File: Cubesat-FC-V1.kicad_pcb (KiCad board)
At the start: 2 copper layers, 109 parts, among them SW1 SW_Button, SW2 SW_SPDT, SW3 SW_SPDT, U1 MMC5983MA, U10 W25Q128JVS, U11 W25Q128JVS, U3 W25Q128JVS, U5 STM32H757BITx, U8 W25Q128JVS, U9 W25Q128JVS, Y1 ASCO, Y3 ASE-xxxMHz

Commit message: Beginnings of routing
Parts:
- removed the D1 at (136.2, 69.5)
- removed the D1 at (141.4, 100.2)
- removed the D2 at (136.2, 72.1)
- removed the D2 at (141.4, 102.8)
- removed the D3 at (141.4, 105.4)
- removed the D3 at (136.2, 74.7)
- removed the D4 at (141.4, 108.0)
- removed the D4 at (136.2, 77.2)
- removed the D5 at (136.2, 79.8)
- removed the D5 at (141.4, 110.6)
- removed the D6 at (136.2, 82.4)
- removed the D6 at (141.4, 113.2)
- removed JP1, JP4: Jumper, Jumper:SolderJumper-3_P1.3mm_Open_RoundedPad1.0x1.5mm
- removed the JP2 at (146.2, 100.7)
- removed the JP2 at (141.1, 79.8)
- removed the R1 at (137.9, 99.9)
- removed the R1 at (139.7, 71.2)
- removed the R3 at (137.9, 101.9)
- removed the R3 at (142.6, 69.2)
- removed the R4 at (142.6, 71.2)
- removed the R4 at (137.9, 103.9)
- removed the R5 at (137.9, 105.9)
- removed the R5 at (142.6, 73.2)
- removed the R6 at (137.9, 107.9)
- removed the R6 at (145.5, 69.2)
- removed the R7 at (137.9, 109.9)
- removed the R7 at (145.5, 71.2)
- removed the R8 at (137.9, 111.9)
- removed the R8 at (145.5, 73.2)
- removed the SW1 at (141.6, 84.2)
- removed the SW1 at (152.4, 112.4)
- added BZ1: Buzzer, Buzzer_Beeper:Buzzer_Murata_PKMCS0909E, F.Cu at (20.0, 22.0)
- added C59: 10n, Capacitor_SMD:C_0402_1005Metric, F.Cu at (156.1, 112.4)
- added C60: 2.2u, Capacitor_SMD:C_0402_1005Metric, F.Cu at (154.2, 118.4)
- added C61: 0.1u, Capacitor_SMD:C_0402_1005Metric, F.Cu at (156.1, 118.4)
- added C62: 10n, Capacitor_SMD:C_0402_1005Metric, F.Cu at (156.1, 119.4)
- added C63: 10u, Capacitor_SMD:C_0402_1005Metric, F.Cu at (164.3, 104.6)
- added C64: 1u, Capacitor_SMD:C_0402_1005Metric, F.Cu at (164.4, 120.4)
- added C65: 10n, Capacitor_SMD:C_0402_1005Metric, F.Cu at (162.5, 110.0)
- added C66: 0.1u, Capacitor_SMD:C_0402_1005Metric, B.Cu at (136.2, 78.9)
- added C67: 0.1u, Capacitor_SMD:C_0402_1005Metric, B.Cu at (136.2, 84.9)
- added C68: 0.1u, Capacitor_SMD:C_0402_1005Metric, B.Cu at (137.5, 89.4)
- added C69: 0.1u, Capacitor_SMD:C_0402_1005Metric, B.Cu at (136.2, 96.9)
- added C70: 10u, Capacitor_SMD:C_0402_1005Metric, B.Cu at (138.9, 67.9)
- added C71: 10u, Capacitor_SMD:C_0402_1005Metric, F.Cu at (141.9, 63.8)
- added C72: 10u, Capacitor_SMD:C_0402_1005Metric, B.Cu at (132.9, 67.9)
- added C73: 10u, Capacitor_SMD:C_0402_1005Metric, F.Cu at (135.9, 63.8)
- added C74: 10u, Capacitor_SMD:C_0402_1005Metric, F.Cu at (86.2, 93.8)
- added C75: 0.1u, Capacitor_SMD:C_0402_1005Metric, F.Cu at (86.2, 95.8)
- added C76: 0.1u, Capacitor_SMD:C_0402_1005Metric, F.Cu at (86.2, 97.8)
- added C77: 10u, Capacitor_SMD:C_0402_1005Metric, F.Cu at (86.2, 99.7)
- added D1: LED_G, LED_SMD:LED_0603_1608Metric, F.Cu at (17.8, 28.5)
- added D2: LED_G, LED_SMD:LED_0603_1608Metric, F.Cu at (17.8, 31.1)
- added D3: LED_G, LED_SMD:LED_0603_1608Metric, F.Cu at (17.8, 33.6)
- added D4: LED_G, LED_SMD:LED_0603_1608Metric, F.Cu at (17.8, 36.2)
- added D5: LED_G, LED_SMD:LED_0603_1608Metric, F.Cu at (17.8, 38.8)
- added D6: LED_G, LED_SMD:LED_0603_1608Metric, F.Cu at (17.8, 41.4)
- added D7: LED_G, LED_SMD:LED_0603_1608Metric, F.Cu at (89.7, 100.4)
- added D8: LED_R, LED_SMD:LED_0603_1608Metric, F.Cu at (89.7, 103.0)
- added H1: M3, MountingHole:MountingHole_3.2mm_M3_ISO7380_Pad_TopBottom, F.Cu at (113.5, 58.5)
- added H2: M3, MountingHole:MountingHole_3.2mm_M3_ISO7380_Pad_TopBottom, F.Cu at (113.5, 123.5)
- added H3: M3, MountingHole:MountingHole_3.2mm_M3_ISO7380_Pad_TopBottom, F.Cu at (169.5, 58.5)
- added H4: M3, MountingHole:MountingHole_3.2mm_M3_ISO7380_Pad_TopBottom, F.Cu at (169.5, 123.5)
- added J1: Conn_01x03_Pin, Connector_Molex:Molex_Micro-Latch_53253-0370_1x03_P2.00mm_Vertical, F.Cu at (19.1, 82.6)
- added J10: Conn_01x04_Pin, Connector_Molex:Molex_Micro-Latch_53253-0470_1x04_P2.00mm_Vertical, F.Cu at (19.1, 44.8)
- added J11: USB_C_Receptacle_USB2.0_14P, Connector_USB:USB_C_Receptacle_GCT_USB4105-xx-A_16P_TopMnt_Horizontal, F.Cu at (42.0, 74.7)
- added J12: Conn_01x03_Pin, Connector_Molex:Molex_Micro-Latch_53253-0370_1x03_P2.00mm_Vertical, F.Cu at (71.0, 62.4)
- added J13: Conn_01x03_Pin, Connector_Molex:Molex_Micro-Latch_53253-0370_1x03_P2.00mm_Vertical, F.Cu at (71.0, 68.1)
- added J14: Conn_01x03_Pin, Connector_Molex:Molex_Micro-Latch_53253-0370_1x03_P2.00mm_Vertical, F.Cu at (71.0, 73.8)
- added J15: Conn_01x03_Pin, Connector_Molex:Molex_Micro-Latch_53253-0370_1x03_P2.00mm_Vertical, F.Cu at (71.0, 79.5)
- added J3: Conn_01x03_Pin, Connector_Molex:Molex_Micro-Latch_53253-0370_1x03_P2.00mm_Vertical, F.Cu at (19.1, 88.3)
- added J4: Conn_01x04_Pin, Connector_Molex:Molex_Micro-Latch_53253-0470_1x04_P2.00mm_Vertical, F.Cu at (19.1, 49.8)
- added J5: Conn_01x04_Pin, Connector_Molex:Molex_Micro-Latch_53253-0470_1x04_P2.00mm_Vertical, F.Cu at (19.1, 55.5)
- added J6: Conn_01x04_Pin, Connector_Molex:Molex_Micro-Latch_53253-0470_1x04_P2.00mm_Vertical, F.Cu at (19.1, 61.2)
- added J7: USB_C_Receptacle_USB2.0_14P, Connector_USB:USB_C_Receptacle_GCT_USB4105-xx-A_16P_TopMnt_Horizontal, F.Cu at (21.9, 75.4)
- added J8: Conn_01x04_Pin, Connector_Molex:Molex_Micro-Latch_53253-0470_1x04_P2.00mm_Vertical, F.Cu at (19.1, 66.9)
- added J9: Micro_SD_Card, Connector_Card:microSD_HC_Hirose_DM3D-SF, F.Cu at (166.4, 95.5)
- added JP2: Jumper_3_Open, Jumper:SolderJumper-3_P1.3mm_Open_RoundedPad1.0x1.5mm, F.Cu at (45.1, 15.9)
- added JP6: Jumper, Jumper:SolderJumper-3_P1.3mm_Open_RoundedPad1.0x1.5mm, F.Cu at (49.1, 38.4)
- added JP7: Jumper, Jumper:SolderJumper-3_P1.3mm_Open_RoundedPad1.0x1.5mm, F.Cu at (54.8, 30.7)
- added JP8: Jumper, Jumper:SolderJumper-3_P1.3mm_Open_RoundedPad1.0x1.5mm, F.Cu at (54.8, 34.5)
- added JP9: Jumper, Jumper:SolderJumper-3_P1.3mm_Open_RoundedPad1.0x1.5mm, F.Cu at (54.8, 38.4)
- added R1: R_Small, Resistor_SMD:R_0402_1005Metric, F.Cu at (21.6, 28.4)
- added R10: 1k, Resistor_SMD:R_0402_1005Metric, F.Cu at (18.8, 125.5)
- added R11: R_Small, Resistor_SMD:R_0402_1005Metric, F.Cu at (18.8, 127.5)
- added R12: 100, Resistor_SMD:R_0402_1005Metric, F.Cu at (61.5, 15.9)
- added R13: 30.9k, Resistor_SMD:R_0402_1005Metric, F.Cu at (37.3, 122.0)
- added R14: 10k, Resistor_SMD:R_0402_1005Metric, F.Cu at (37.3, 124.0)
- added R15: 68k, Resistor_SMD:R_0402_1005Metric, F.Cu at (37.3, 126.0)
- added R16: R_Small, Resistor_SMD:R_0402_1005Metric, F.Cu at (44.0, 37.2)
- added R17: R_Small, Resistor_SMD:R_0402_1005Metric, F.Cu at (44.0, 39.2)
- added R18: 120, Resistor_SMD:R_0402_1005Metric, F.Cu at (138.9, 62.7)
- added R19: 120, Resistor_SMD:R_0402_1005Metric, F.Cu at (132.9, 62.7)
- added R20: 20k, Resistor_SMD:R_0402_1005Metric, F.Cu at (83.3, 93.8)
- added R21: 47k, Resistor_SMD:R_0402_1005Metric, F.Cu at (83.3, 95.8)
- added R22: 20k, Resistor_SMD:R_0402_1005Metric, F.Cu at (83.3, 97.8)
- added R23: 20k, Resistor_SMD:R_0402_1005Metric, F.Cu at (83.3, 99.8)
- added R24: 5.1k, Resistor_SMD:R_0402_1005Metric, F.Cu at (37.6, 80.4)
- added R25: 5.1k, Resistor_SMD:R_0402_1005Metric, F.Cu at (37.6, 82.4)
- added R3: R_Small, Resistor_SMD:R_0402_1005Metric, F.Cu at (21.6, 32.4)
- added R4: R_Small, Resistor_SMD:R_0402_1005Metric, F.Cu at (21.6, 34.4)
- added R5: R_Small, Resistor_SMD:R_0402_1005Metric, F.Cu at (21.6, 36.4)
- added R6: R_Small, Resistor_SMD:R_0402_1005Metric, F.Cu at (21.6, 38.4)
- added R7: 5.1k, Resistor_SMD:R_0402_1005Metric, F.Cu at (14.7, 71.2)
- added R8: 5.1k, Resistor_SMD:R_0402_1005Metric, F.Cu at (14.7, 73.2)
- added SW1: SW_SPDT, Button_Switch_THT:SW_CK_JS202011CQN_DPDT_Straight, F.Cu at (61.6, 18.1)
- added SW4: SW_Button, Button_Switch_SMD:SW_SPST_PTS810, F.Cu at (37.9, 38.1)
- added SW5: SW_SPDT, Button_Switch_THT:SW_CK_JS202011CQN_DPDT_Straight, F.Cu at (36.0, 25.2)
- added SW6: SW_SPDT, Button_Switch_THT:SW_CK_JS202011CQN_DPDT_Straight, F.Cu at (36.0, 30.8)
- added TP1: TestPoint, TestPoint:TestPoint_Pad_D1.5mm, F.Cu at (16.4, 101.5)
- added TP10: TestPoint, TestPoint:TestPoint_Pad_D1.5mm, F.Cu at (27.0, 97.6)
- added TP11: TestPoint, TestPoint:TestPoint_Pad_D1.5mm, F.Cu at (27.0, 101.2)
- added TP12: TestPoint, TestPoint:TestPoint_Pad_D1.5mm, F.Cu at (27.0, 104.7)
- added TP13: TestPoint, TestPoint:TestPoint_Pad_D1.5mm, F.Cu at (30.6, 87.0)
- added TP14: TestPoint, TestPoint:TestPoint_Pad_D1.5mm, F.Cu at (30.6, 90.5)
- added TP15: TestPoint, TestPoint:TestPoint_Pad_D1.5mm, F.Cu at (30.6, 94.0)
- added TP16: TestPoint, TestPoint:TestPoint_Pad_D1.5mm, F.Cu at (30.6, 97.6)
- added TP17: TestPoint, TestPoint:TestPoint_Pad_D1.5mm, F.Cu at (30.6, 101.2)
- added TP18: TestPoint, TestPoint:TestPoint_Pad_D1.5mm, F.Cu at (30.6, 104.7)
- added TP19: TestPoint, TestPoint:TestPoint_Pad_D1.5mm, F.Cu at (34.1, 87.0)
- added TP2: TestPoint, TestPoint:TestPoint_Pad_D1.5mm, F.Cu at (16.4, 105.0)
- added TP20: TestPoint, TestPoint:TestPoint_Pad_D1.5mm, F.Cu at (34.1, 90.5)
- added TP21: TestPoint, TestPoint:TestPoint_Pad_D1.5mm, F.Cu at (34.1, 94.0)
- added TP22: TestPoint, TestPoint:TestPoint_Pad_D1.5mm, F.Cu at (34.1, 97.6)
- added TP23: TestPoint, TestPoint:TestPoint_Pad_D1.5mm, F.Cu at (34.1, 101.2)
- added TP24: TestPoint, TestPoint:TestPoint_Pad_D1.5mm, F.Cu at (34.1, 104.7)
- added TP3: TestPoint, TestPoint:TestPoint_Pad_D1.5mm, F.Cu at (19.9, 101.5)
- added TP4: TestPoint, TestPoint:TestPoint_Pad_D1.5mm, F.Cu at (19.9, 105.0)
- added TP5: TestPoint, TestPoint:TestPoint_Pad_D1.5mm, F.Cu at (23.5, 101.5)
- added TP6: TestPoint, TestPoint:TestPoint_Pad_D1.5mm, F.Cu at (23.5, 105.0)
- added TP7: TestPoint, TestPoint:TestPoint_Pad_D1.5mm, F.Cu at (27.0, 87.0)
- added TP8: TestPoint, TestPoint:TestPoint_Pad_D1.5mm, F.Cu at (27.0, 90.5)
- added TP9: TestPoint, TestPoint:TestPoint_Pad_D1.5mm, F.Cu at (27.0, 94.0)
- added U12: W25Q128JVS, Package_SO:SOIC-8_5.3x5.3mm_P1.27mm, B.Cu at (141.4, 80.4)
- added U13: W25Q128JVS, Package_SO:SOIC-8_5.3x5.3mm_P1.27mm, B.Cu at (141.4, 92.4)
- added U14: W25Q128JVS, Package_SO:SOIC-8_5.3x5.3mm_P1.27mm, B.Cu at (141.4, 98.4)
- added U15: MCP2558FD, Package_SO:SOIC-8_3.9x4.9mm_P1.27mm, F.Cu at (138.9, 67.0)
- added U16: MCP2558FD, Package_SO:SOIC-8_3.9x4.9mm_P1.27mm, F.Cu at (132.9, 67.0)
- added U18: CP2102N-Axx-xQFN24, Package_DFN_QFN:QFN-24-1EP_4x4mm_P0.5mm_EP2.6x2.6mm, F.Cu at (90.8, 96.0)
- added U4: STM32H757BITx, Package_QFP:LQFP-208_28x28mm_P0.5mm, F.Cu at (141.0, 89.5)
- added Y2: ASCO, Oscillator:Oscillator_SMD_Abracon_ASCO-4Pin_1.6x1.2mm, F.Cu at (124.3, 93.2)
- C10, C11: value 0.1u -> 100u; footprint Capacitor_SMD:C_0402_1005Metric -> Capacitor_SMD:C_1206_3216Metric
- C2, C8, C9: value 0.1u -> 47u; footprint Capacitor_SMD:C_0402_1005Metric -> Capacitor_SMD:C_1206_3216Metric
- C24, C30, C50: value 1u -> 0.1u
- C25, C26, C27, C28: value 2.2u -> 0.1u
- C3, C7: value 0.1u -> 10u
- C32: value 4.7u -> 0.1u
- C33, C34: value ?? -> 0.1u
- C38: value 10n -> 0.1u
- C39: value 0.1u -> 4.7u
- C40: value 10n -> 1u
- C41, C44, C57: value 0.1u -> 2.2u
- C43: value 10n -> 2.2u
- C45: value 2.2u -> 1u
- C46: value 10u -> 0.1u
- C47: value 0.1u -> ??
- C48: value 1u -> ??
- C49: value 10u -> 1u; moved to B.Cu
- C5: value 0.1u -> 33n
- C51, U11: moved to B.Cu
- C53: value 1u -> 10u
- C56: value 0.1u -> 1u
- JP3, JP5: value Jumper -> Jumper_3_Open
- R9: value R_Small -> 1k
- SW2: footprint Button_Switch_SMD:SW_DPDT_CK_JS202011JCQN -> Button_Switch_THT:SW_CK_JS202011CQN_DPDT_Straight
- SW3: value SW_SPDT -> SW_DIP_x04; footprint Button_Switch_SMD:SW_DPDT_CK_JS202011JCQN -> Button_Switch_THT:SW_DIP_SPSTx04_Slide_6.7x11.72mm_W7.62mm_P2.54mm_LowProfile
- U1: value MMC5983MA -> ~; footprint Package_LGA:LGA-16_3x3mm_P0.5mm -> Connector_PinSocket_2.54mm:PinSocket_2x10_P2.54mm_Vertical
- U10: value W25Q128JVS -> ~; footprint Package_SO:SOIC-8_5.3x5.3mm_P1.27mm -> SCH16T:SCH16T
- U2: value ~ -> TPS2117DRL; footprint Package_SO:TSOP-II-54_22.2x10.16mm_P0.8mm -> Package_TO_SOT_SMD:SOT-583-8
- U3: value W25Q128JVS -> TPS62933; footprint Package_SO:SOIC-8_5.3x5.3mm_P1.27mm -> Package_TO_SOT_SMD:SOT-583-8
- U5: value STM32H757BITx -> ~; footprint Package_QFP:LQFP-208_28x28mm_P0.5mm -> Package_SO:TSOP-II-54_22.2x10.16mm_P0.8mm
- U6: value ~ -> W25Q128JVS; footprint Package_LGA:LGA-14_3x2.5mm_P0.5mm_LayoutBorder3x4y -> Package_SO:SOIC-8_5.3x5.3mm_P1.27mm; moved to B.Cu
- U8: value W25Q128JVS -> MMC5983MA; footprint Package_SO:SOIC-8_5.3x5.3mm_P1.27mm -> Package_LGA:LGA-16_3x3mm_P0.5mm
- U9: value W25Q128JVS -> ~; footprint Package_SO:SOIC-8_5.3x5.3mm_P1.27mm -> Package_LGA:LGA-14_3x2.5mm_P0.5mm_LayoutBorder3x4y
- Y1: value ASCO -> 32.768KHZ; footprint Oscillator:Oscillator_SMD_Abracon_ASCO-4Pin_1.6x1.2mm -> Crystal:Crystal_SMD_Abracon_ABM3-2Pin_5.0x3.2mm
- moved SW2 143.8 mm to (37.0, 18.6)
- moved U3 141.0 mm to (36.3, 130.8)
- moved JP5 135.6 mm to (50.8, 15.9)
- moved JP3 132.0 mm to (45.1, 19.7)
- moved C11 128.1 mm to (32.8, 129.8)
- moved C10 127.4 mm to (32.8, 126.5)
- moved C9 126.6 mm to (32.8, 123.1)
- moved R2 125.6 mm to (21.6, 30.4)
- moved C1 124.0 mm to (29.1, 116.8)
- moved C3 123.0 mm to (29.1, 118.8)
- moved C4 123.0 mm to (29.1, 120.8)
- moved C5 123.0 mm to (29.1, 122.7)
- moved C6 123.0 mm to (29.1, 124.7)
- moved C7 123.0 mm to (29.1, 126.7)
- moved C2 119.6 mm to (32.8, 116.4)
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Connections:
- C1 pad 1: +3.3V -> Net-(U3-BST)
- C1 pad 2: GND -> /3V3_BUCK
- C10 pad 1: +3.3V -> /3V3_BUCK
- C11 pad 1: +3.3V -> /3V3_BUCK
- C16 pad 1: +3.3VA -> +3.3V
- C16 pad 2: GND -> unconnected-(C16-Pad2)
- C2 pad 1: +3.3V -> /BUCKVIN
- C24 pad 1: +3.3VA -> +3.3V
- C25 pad 1: /STM32H747/VCAP -> +3.3V
- C26 pad 1: /STM32H747/VCAP -> +3.3V
- C27 pad 1: /STM32H747/VCAP -> +3.3V
- C28 pad 1: /STM32H747/VCAPDSI -> +3.3V
- C29 pad 1: /NRST -> +3.3V
- C3 pad 1: +3.3V -> /BUCKVIN
- C30 pad 1: +3.3VA -> +3.3V
- C31 pad 1: +3.3VA -> +3.3V
- C33 pad 1: /STM32H747/LFOSC_OUT -> +3.3V
- C34 pad 1: /STM32H747/LFOSC_IN -> /NRST
- C35 pad 1: +3.3V -> +3.3VA
- C36 pad 1: +3.3V -> +3.3VA
- C37 pad 1: +3.3V -> +3.3VA
- C38 pad 1: +3.3V -> +3.3VA
- C4 pad 1: +3.3V -> /BUCKVIN
- C41 pad 1: +3.3V -> /STM32H747/VCAPDSI
- C42 pad 1: +3.3V -> /STM32H747/VCAP
- C43 pad 1: +3.3V -> /STM32H747/VCAP
- C44 pad 1: +3.3V -> /STM32H747/VCAP
- C46 pad 1: Net-(U1-CAP) -> +3.3V
- C47 pad 1: +3.3V -> /STM32H747/LFOSC_IN
- C48 pad 1: Net-(U4-VREGD) -> /STM32H747/LFOSC_OUT
- C49 pad 1: Net-(U4-VREGA) -> +3.3V
- C5 pad 1: +3.3V -> Net-(U3-SS)
- C5 pad 2: unconnected-(C5-Pad2) -> GND
- C53 pad 1: +3.3V -> Net-(U8-CAP)
- C6 pad 1: +3.3V -> /3V3_BUCK
- C7 pad 1: +3.3V -> /3V3_BUCK
- C8 pad 1: +3.3V -> /3V3_BUCK
- C9 pad 1: +3.3V -> /3V3_BUCK
- JP3 pad 1: Net-(JP3-A) -> /3V3_EXT
- JP3 pad 2: Net-(JP3-C) -> +3.3V
- JP3 pad 3: Net-(JP3-B) -> /3V3_BUCK
- JP5 pad 1: +3.3V -> GND
- JP5 pad 2: unconnected-(JP5-C-Pad2) -> Net-(JP2-A)
- JP5 pad 3: GND -> /BUCKVIN
- R2 pad 1: /STM32H747/PDR_EN -> Net-(D2-K)
- R2 pad 2: Net-(JP2-C) -> GND
- R9 pad 1: /PDR_EN -> Net-(U2-PR1)
- R9 pad 2: Net-(JP3-C) -> +5V
- SW2 pad 1: +3.3V -> GND
- SW2 pad 2: Net-(JP3-B) -> Net-(JP2-B)
- SW2 pad 3: GND -> /BUCKVIN
- SW3 pad 1: +3.3V -> /PIN_GPIO_CFG_0
- SW3 pad 2: Net-(JP2-B) -> /PIN_GPIO_CFG_1
- SW3 pad 3: GND -> /PIN_GPIO_CFG_2
- SW3 pad 4: (no net) -> /PIN_GPIO_CFG_3
- SW3 pad 5: (no net) -> GND
- SW3 pad 6: (no net) -> GND
- U1 pad 1: /Inertial Measurement System/SPI_SCK -> +3.3V
- U1 pad 10: Net-(U1-CAP) -> /TRST
- U1 pad 12: unconnected-(U1-NC-Pad12) -> /SWD_TRACE_D0
- U1 pad 13: +3.3V -> GND
- U1 pad 14: unconnected-(U1-NC-Pad14) -> /SWD_TRACE_D1
- U1 pad 15: unconnected-(U1-INT-Pad15) -> GND
- U1 pad 16: /Inertial Measurement System/SPI_COPI -> /SWD_TRACE_D2
- U1 pad 2: +3.3V -> /SWD_TMS/SWDIO
- U1 pad 3: unconnected-(U1-NC-Pad3) -> GND
- U1 pad 4: /Inertial Measurement System/SPI_CS_MAG -> /SWD_TCK/SWCLK
- U1 pad 5: /Inertial Measurement System/SPI_CIPO -> GND
- U1 pad 6: unconnected-(U1-NC-Pad6) -> /SWD_TDO/SWO
- U1 pad 7: unconnected-(U1-NC-Pad7) -> GND
- U1 pad 8: unconnected-(U1-NC-Pad8) -> /SWD_TDI
- U10 pad 1: /Flash Storage/SPI_CS_CATALOG1 -> GND
- U10 pad 2: /Flash Storage/SPI_CIPO -> unconnected-(U10-RSV-Pad2)
- U10 pad 3: unconnected-(U10-IO2-Pad3) -> GND
- U10 pad 5: /Flash Storage/SPI_COPI -> unconnected-(U10-RSV-Pad5)
- U10 pad 6: /Flash Storage/SPI_CLK -> +3.3V
- U11 pad 1: /Flash Storage/SPI_CS_CATALOG2 -> /SPI_CS_CATALOG0
- U11 pad 2: /Flash Storage/SPI_CIPO -> /SPI1_CIPO
- U11 pad 5: /Flash Storage/SPI_COPI -> /SPI1_COPI
- U11 pad 6: /Flash Storage/SPI_CLK -> /SPI1_SCK
- U2 pad 1: +3.3V -> GND
- U2 pad 2: /SDRAM/FMCD0 -> /BUCKVIN
- U2 pad 3: +3.3V -> +5V
- U2 pad 4: /SDRAM/FMCD1 -> Net-(U2-PR1)
- U2 pad 5: /SDRAM/FMCD2 -> +5V
- U2 pad 6: GND -> VBUS
- U2 pad 7: /SDRAM/FMCD3 -> /BUCKVIN
- U2 pad 8: /SDRAM/FMCD4 -> Net-(U2-ST)
- U3 pad 1: /Flash Storage/SPI_CS_DATALOG0 -> Net-(U3-RT)
- U3 pad 2: /Flash Storage/SPI_CIPO -> /BUCK_EN
- U3 pad 3: unconnected-(U3-IO2-Pad3) -> /BUCKVIN
- U3 pad 5: /Flash Storage/SPI_COPI -> /3V3_BUCK
- U3 pad 6: /Flash Storage/SPI_CLK -> Net-(U3-BST)
- U3 pad 7: unconnected-(U3-IO3-Pad7) -> Net-(U3-SS)
- U3 pad 8: +3.3V -> Net-(U3-FB)
- U5 pad 1: /SWD_TRACE_CK -> +3.3V
- U5 pad 10: unconnected-(U5-PC13-Pad10) -> /SDRAM/FMCD5
- U5 pad 11: /STM32H747/LFOSC_IN -> /SDRAM/FMCD6
- U5 pad 12: /STM32H747/LFOSC_OUT -> GND
- U5 pad 13: /PIN_PROC0GP0 -> /SDRAM/FMCD7
- U5 pad 14: /PIN_PROC0GP1 -> +3.3V
- U5 pad 15: /STM32H747/PIN_CONFIG_0 -> /STM32H747/FMCNBL0
- U5 pad 16: GND -> /SDRAM/FMCWE
- U5 pad 17: +3.3V -> /SDRAM/FMCCAS
- U5 pad 18: GND -> /SDRAM/FMCRAS
- U5 pad 19: unconnected-(U5-VLXSMPS-Pad19) -> /SDRAM/FMC_CS
- U5 pad 2: /SWD_TRACE_D0 -> /SDRAM/FMCD0
- U5 pad 20: unconnected-(U5-VDDSMPS-Pad20) -> /STM32H747/FMCBA0
- U5 pad 21: unconnected-(U5-VFBSMPS-Pad21) -> /STM32H747/FMCBA1
- U5 pad 22: /STM32H747/FMCA0 -> /SDRAM/FMCA10
- U5 pad 23: /STM32H747/FMCA1 -> /SDRAM/FMCA0
- U5 pad 24: /STM32H747/FMCA2 -> /SDRAM/FMCA1
- U5 pad 25: /STM32H747/FMCA3 -> /SDRAM/FMCA2
- U5 pad 26: /STM32H747/FMCA4 -> /SDRAM/FMCA3
- U5 pad 27: /STM32H747/FMCA5 -> +3.3V
- U5 pad 29: +3.3V -> /SDRAM/FMCA4
- U5 pad 3: /SWD_TRACE_D1 -> +3.3V
- U5 pad 30: /QSPI Flash/QSPI_D3 -> /SDRAM/FMCA5
- U5 pad 31: /QSPI Flash/QSPI_D2 -> /SDRAM/FMCA6
- U5 pad 32: /QSPI Flash/QSPI_D0 -> /SDRAM/FMCA7
- U5 pad 33: /QSPI Flash/QSPI_D1 -> /SDRAM/FMCA8
- U5 pad 34: /STM32H747/QSPI_CLK -> /SDRAM/FMCA9
- U5 pad 35: /STM32H747/HFOSC_IN -> /SDRAM/FMCA11
- U5 pad 36: /STM32H747/PIN_CONFIG_2 -> /SDRAM/FMCA12
- U5 pad 37: /NRST -> /SDRAM/FMCCKE
- U5 pad 38: /Inertial Measurement System/SPI_CS_IMU_PRI -> /SDRAM/FMCCLK
- U5 pad 39: /Inertial Measurement System/SPI_CS_IMU_SEC0 -> /STM32H747/FMCNBL1
- U5 pad 4: /SWD_TRACE_D2 -> /SDRAM/FMCD1
- U5 pad 40: /Inertial Measurement System/SPI_CS_IMU_SEC1 -> unconnected-(U5-NC-Pad40)
- U5 pad 41: /Inertial Measurement System/SPI_CS_MAG -> GND
- U5 pad 42: GND -> /SDRAM/FMCD8
- U5 pad 43: +3.3VA -> +3.3V
- U5 pad 44: +3.3VA -> /SDRAM/FMCD9
- U5 pad 45: unconnected-(U5-PA0-Pad45) -> /SDRAM/FMCD10
- U5 pad 46: unconnected-(U5-PA1-Pad46) -> GND
- U5 pad 47: unconnected-(U5-PA2-Pad47) -> /SDRAM/FMCD11
- U5 pad 48: /STM32H747/PIN_CONFIG_3 -> /SDRAM/FMCD12
- U5 pad 5: /SWD_TRACE_D3 -> /SDRAM/FMCD2
- U5 pad 50: GND -> /SDRAM/FMCD13
- U5 pad 51: unconnected-(U5-PH3-Pad51) -> /SDRAM/FMCD14
- U5 pad 52: /ISC2_SCL -> GND
- U5 pad 53: /I2C2_SDA -> /SDRAM/FMCD15
- U5 pad 54: unconnected-(U5-PA3-Pad54) -> GND
- U5 pad 7: +3.3V -> /SDRAM/FMCD3
- U5 pad 8: +3.3V -> /SDRAM/FMCD4
- U5 pad 9: /PIN_PROC0BUSY -> +3.3V
- U6 pad 1: /Inertial Measurement System/SPI_CIPO -> /QSPI Flash/QSPI_FLASH0_CS
- U6 pad 2: unconnected-(U6-RESV-Pad2) -> /QSPI Flash/QSPI_D1
- U6 pad 3: unconnected-(U6-RESV-Pad3) -> /QSPI Flash/QSPI_D2
- U6 pad 4: unconnected-(U6-INT1/INT-Pad4) -> GND
- U6 pad 5: +3.3V -> /QSPI Flash/QSPI_D0
- U6 pad 6: GND -> /STM32H747/QSPI_CLK
- U6 pad 7: unconnected-(U6-RESV-Pad7) -> /QSPI Flash/QSPI_D3
- U7 pad 1: /Inertial Measurement System/SPI_CIPO -> /SPI2_CIPO
- U7 pad 12: /Inertial Measurement System/SPI_CS_IMU_SEC1 -> /SPI_CS_IMU_SEC0
- U7 pad 13: /Inertial Measurement System/SPI_SCK -> /SPI2_SCK
- U7 pad 14: /Inertial Measurement System/SPI_COPI -> /SPI2_COPI
- U8 pad 1: /Flash Storage/SPI_CS_CATALOG3 -> /SPI2_SCK
- U8 pad 2: /Flash Storage/SPI_CIPO -> +3.3V
- U8 pad 4: GND -> /SPI_CS_MAG
- U8 pad 5: /Flash Storage/SPI_COPI -> /SPI2_CIPO
- U8 pad 6: /Flash Storage/SPI_CLK -> unconnected-(U8-NC-Pad6)
- U8 pad 8: +3.3V -> unconnected-(U8-NC-Pad8)
- U9 pad 1: /QSPI Flash/QSPI_FLASH0_CS -> /SPI2_CIPO
- U9 pad 2: /QSPI Flash/QSPI_D1 -> unconnected-(U9-RESV-Pad2)
- U9 pad 3: /QSPI Flash/QSPI_D2 -> unconnected-(U9-RESV-Pad3)
- U9 pad 4: GND -> unconnected-(U9-INT1/INT-Pad4)
- U9 pad 5: /QSPI Flash/QSPI_D0 -> +3.3V
- U9 pad 6: /STM32H747/QSPI_CLK -> GND
- U9 pad 7: /QSPI Flash/QSPI_D3 -> unconnected-(U9-RESV-Pad7)
- Y1 pad 1: +3.3V -> /STM32H747/LFOSC_IN
- Y1 pad 2: GND -> /STM32H747/LFOSC_OUT
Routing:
- net GND: track 0.00 -> 58.2 mm, vias 0 -> 39
- net +3.3V: track 0.00 -> 53.6 mm, vias 0 -> 25
- net /SDRAM/FMCCLK: track 0.00 -> 42.7 mm, vias 0 -> 2
- net /SDRAM/FMCA12: track 0.00 -> 38.7 mm, vias 0 -> 2
- net /STM32H747/FMCBA1: track 0.00 -> 35.9 mm, vias 0 -> 2
- net /STM32H747/FMCBA0: track 0.00 -> 35.0 mm, vias 0 -> 2
- net /SDRAM/FMCA5: track 0.00 -> 34.5 mm, vias 0 -> 2
- net /SDRAM/FMCA4: track 0.00 -> 33.5 mm, vias 0 -> 2
- net /SPI2_CIPO: track 0.00 -> 30.8 mm, vias 0 -> 5
- net /SPI2_SCK: track 0.00 -> 29.9 mm, vias 0 -> 5
- net /SPI1_SCK: track 0.00 -> 29.9 mm, vias 0 -> 4
- net /SPI1_COPI: track 0.00 -> 28.8 mm, vias 0 -> 4
- net /SPI1_CIPO: track 0.00 -> 28.3 mm, vias 0 -> 4
- net /SPI2_COPI: track 0.00 -> 26.6 mm, vias 0 -> 5
- net /SDRAM/FMCA0: track 0.00 -> 26.1 mm, vias 0 -> 2
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- added copper zone on In2.Cu, net +3.3V
- added copper zone on In1.Cu, net GND
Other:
- board outline added: 63 x 72 mm
- copper layers 2 -> 4

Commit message: more routing
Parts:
- removed C11: 100u, Capacitor_SMD:C_1206_3216Metric
- removed J14, J15: Conn_01x03_Pin, Connector_Molex:Molex_Micro-Latch_53253-0370_1x03_P2.00mm_Vertical
- removed JP3, JP5: Jumper_3_Open, Jumper:SolderJumper-3_P1.3mm_Open_RoundedPad1.0x1.5mm
- removed JP6, JP7, JP8, JP9: Jumper, Jumper:SolderJumper-3_P1.3mm_Open_RoundedPad1.0x1.5mm
- added J16: Screw_Terminal_01x02, TerminalBlock_Phoenix:TerminalBlock_Phoenix_MKDS-1,5-2-5.08_1x02_P5.08mm_Horizontal, F.Cu at (109.8, 59.0)
- added L1: 5.6u, Inductor_SMD:L_Coilcraft_XAL7070-XXX, F.Cu at (125.0, 63.5)
- added kibuzzard-69B64A9E: G***, kibuzzard-69B64A9E, F.Cu at (121.2, 75.9)
- added kibuzzard-69B64AB5: G***, kibuzzard-69B64AB5, F.Cu at (110.0, 71.2)
- added kibuzzard-69B64C2A: G***, kibuzzard-69B64C2A, F.Cu at (123.4, 58.1)
- added kibuzzard-69B64C2A: G***, kibuzzard-69B64C2A, F.Cu at (128.4, 58.1)
- added kibuzzard-69B64C48: G***, kibuzzard-69B64C48, F.Cu at (133.5, 58.1)
- added kibuzzard-69B64C48: G***, kibuzzard-69B64C48, F.Cu at (138.5, 58.1)
- added kibuzzard-69B64C5E: G***, kibuzzard-69B64C5E, F.Cu at (144.0, 60.1)
- added kibuzzard-69B64C7E: G***, kibuzzard-69B64C7E, F.Cu at (107.1, 110.3)
- added kibuzzard-69B64C7E: G***, kibuzzard-69B64C7E, F.Cu at (112.1, 110.3)
- added kibuzzard-69B64C8D: G***, kibuzzard-69B64C8D, F.Cu at (116.0, 117.9)
- added kibuzzard-69B64C8D: G***, kibuzzard-69B64C8D, F.Cu at (116.0, 112.9)
- added kibuzzard-69B64D23: G***, kibuzzard-69B64D23, F.Cu at (122.5, 102.6)
- added kibuzzard-69B64D30: G***, kibuzzard-69B64D30, F.Cu at (122.5, 104.0)
- added kibuzzard-69B64D62: G***, kibuzzard-69B64D62, F.Cu at (122.6, 107.4)
- added kibuzzard-69B74E8C: G***, kibuzzard-69B74E8C, F.Cu at (158.3, 61.2)
- added kibuzzard-69B753B2: G***, kibuzzard-69B753B2, F.Cu at (163.9, 71.8)
- added kibuzzard-69B753C8: G***, kibuzzard-69B753C8, F.Cu at (169.8, 61.2)
- added kibuzzard-69B7542C: G***, kibuzzard-69B7542C, F.Cu at (173.5, 64.0)
- added kibuzzard-69B7542C: G***, kibuzzard-69B7542C, F.Cu at (177.0, 96.5)
- added kibuzzard-69B75433: G***, kibuzzard-69B75433, F.Cu at (173.5, 69.0)
- added kibuzzard-69B75433: G***, kibuzzard-69B75433, F.Cu at (177.1, 101.5)
- added kibuzzard-69B75457: G***, kibuzzard-69B75457, F.Cu at (161.8, 93.0)
- added kibuzzard-69B7545E: G***, kibuzzard-69B7545E, F.Cu at (165.6, 93.0)
- added kibuzzard-69B75463: G***, kibuzzard-69B75463, F.Cu at (168.3, 93.0)
- added kibuzzard-69B7546B: G***, kibuzzard-69B7546B, F.Cu at (170.9, 93.0)
- added kibuzzard-69B75470: G***, kibuzzard-69B75470, F.Cu at (173.6, 93.0)
- added kibuzzard-69B755D8: G***, kibuzzard-69B755D8, F.Cu at (115.7, 89.1)
- added kibuzzard-69B755DD: G***, kibuzzard-69B755DD, F.Cu at (115.9, 87.0)
- C3, C4, C6, C7: footprint Capacitor_SMD:C_0402_1005Metric -> Capacitor_SMD:C_1206_3216Metric
- moved D4 155.1 mm to (163.5, 89.5), turned to 180 degrees
- moved R4 154.2 mm to (165.6, 89.5), turned to -90 degrees
- moved D5 153.6 mm to (163.5, 87.5), turned to 180 degrees
- moved R5 152.8 mm to (165.6, 87.5), turned to -90 degrees
- moved D6 152.2 mm to (163.5, 85.5), turned to 180 degrees
- moved R6 151.5 mm to (165.6, 85.5), turned to -90 degrees
- moved SW6 137.3 mm to (167.9, 69.0), turned to 90 degrees
- moved BZ1 136.0 mm to (148.5, 66.5), turned to 180 degrees
- moved SW5 133.3 mm to (161.9, 69.0), turned to 90 degrees
- moved J4 124.6 mm to (143.5, 57.0), turned to 90 degrees
- moved J1 122.5 mm to (138.5, 55.0), turned to 90 degrees
- moved J10 122.4 mm to (120.0, 114.2)
- moved SW3 120.7 mm to (173.3, 95.2), turned to -90 degrees
- moved D2 116.5 mm to (117.7, 90.9)
- moved D3 116.2 mm to (117.7, 92.9)
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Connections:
- C1 pad 2: /3V3_BUCK -> Net-(U3-SW)
- C10 pad 1: /3V3_BUCK -> +3.3V
- C16 pad 2: unconnected-(C16-Pad2) -> GND
- C6 pad 1: /3V3_BUCK -> +3.3V
- C7 pad 1: /3V3_BUCK -> +3.3V
- C8 pad 1: /3V3_BUCK -> +3.3V
- C9 pad 1: /3V3_BUCK -> +3.3V
- JP2 pad 3: Net-(JP2-B) -> /BUCKVIN
- R16 pad 2: Net-(JP8-C) -> Net-(SW5-B)
- R17 pad 2: Net-(JP9-C) -> Net-(SW6-B)
- SW2 pad 2: Net-(JP2-B) -> Net-(JP2-A)
- SW5 pad 2: Net-(JP8-B) -> Net-(SW5-B)
- SW6 pad 2: Net-(JP9-B) -> Net-(SW6-B)
- U3 pad 5: /3V3_BUCK -> Net-(U3-SW)
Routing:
- net /SD Card/CLK: track 0.00 -> 36.2 mm, vias 0 -> 2
- net /SD Card/CMD: track 0.00 -> 35.2 mm, vias 0 -> 2
- net /SD Card/DAT3: track 0.00 -> 32.7 mm, vias 0 -> 2
- net /SD Card/DAT2: track 0.00 -> 31.4 mm, vias 0 -> 2
- net /SD Card/DAT1: track 0.00 -> 24.5 mm, vias 0 -> 2
- net /SD Card/DAT0: track 0.00 -> 23.9 mm, vias 0 -> 2
- net /CAN1_L: track 0.00 -> 21.4 mm
- net /CAN2_L: track 0.00 -> 20.1 mm
- net /CAN1_H: track 0.00 -> 16.9 mm
- net /CAN2_H: track 0.00 -> 14.6 mm
- net GND: track 58.2 -> 67.7 mm, vias 39 -> 47
- net +3.3V: track 53.6 -> 62.4 mm, vias 25 -> 29
- net /USB_FS_DM: track 0.00 -> 8.78 mm
- net /USB_FS_DP: track 0.00 -> 8.42 mm
- net /BUZZER: track 0.00 -> 4.37 mm
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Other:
- board size 63 x 72 mm -> 75 x 75 mm

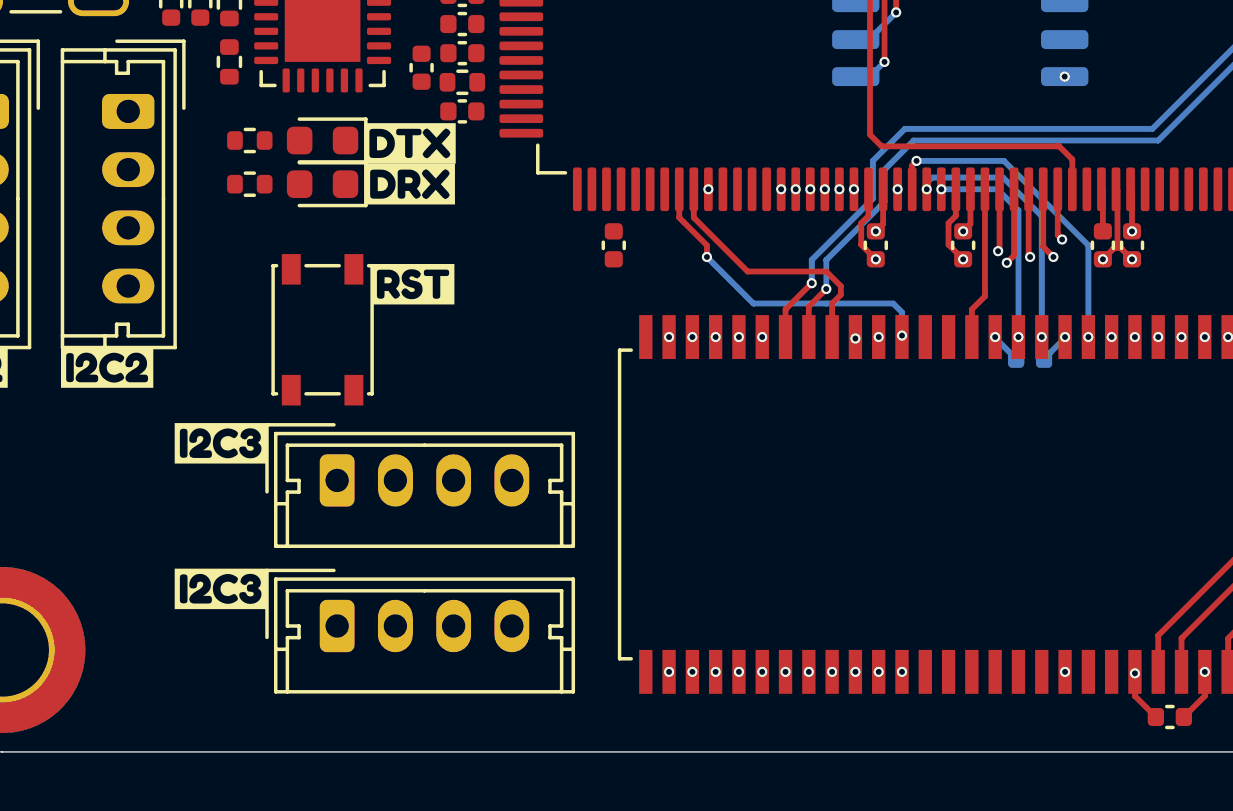
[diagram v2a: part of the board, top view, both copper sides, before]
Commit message: fix SDRAM routing
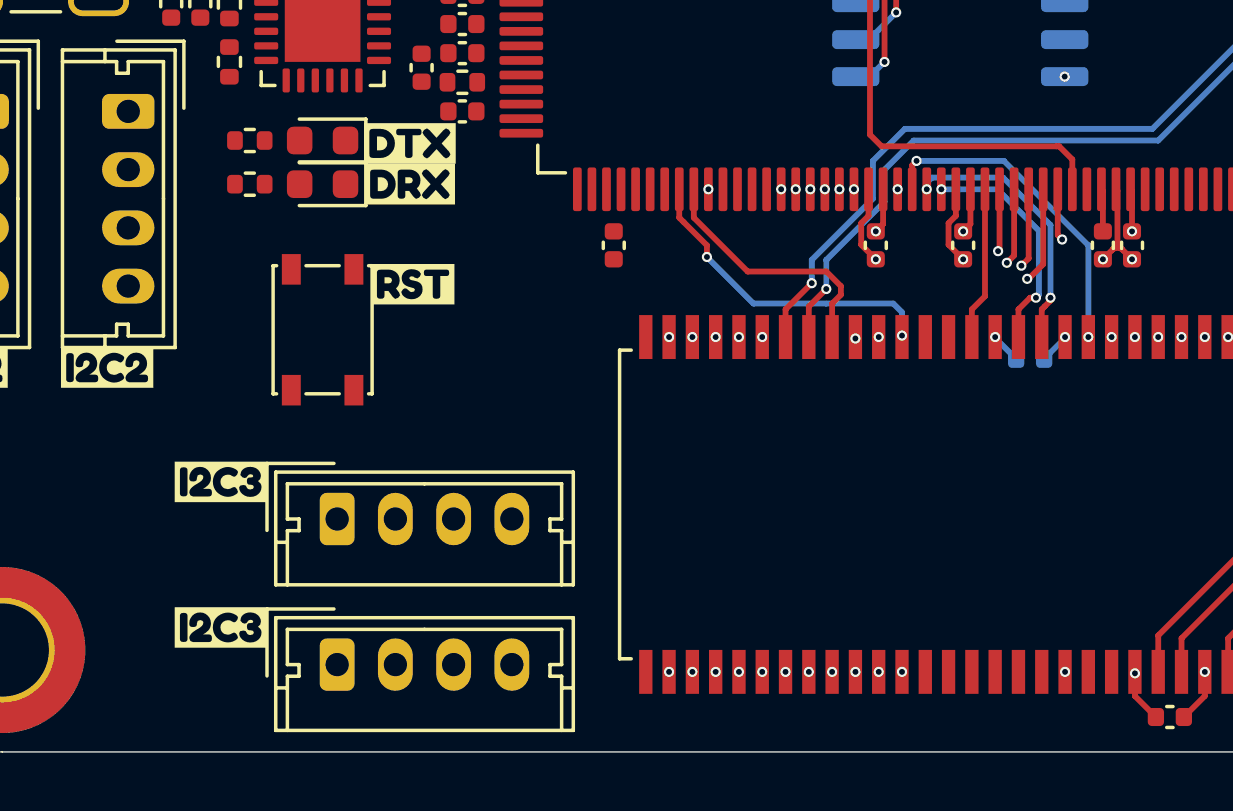
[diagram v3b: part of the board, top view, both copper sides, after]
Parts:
- moved J10 1.33 mm to (120.0, 115.5)
- moved J8 1.33 mm to (120.0, 120.5)
- moved kibuzzard-69B64C8D 1.32 mm to (116.0, 119.2)
- moved kibuzzard-69B64C8D 1.32 mm to (116.0, 114.2)
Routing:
- net /SDRAM/FMCD6: track 7.30 -> 8.00 mm
- net /SDRAM/FMCD11: track 17.3 -> 17.8 mm

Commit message: more routing
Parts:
- added kibuzzard-69B9AFC9: G***, kibuzzard-69B9AFC9, F.Cu at (117.4, 78.4)
- added kibuzzard-69B9BE81: G***, kibuzzard-69B9BE81, F.Cu at (164.6, 84.5)
- added kibuzzard-69B9BE8E: G***, kibuzzard-69B9BE8E, F.Cu at (164.8, 86.5)
- added kibuzzard-69B9BE9C: G***, kibuzzard-69B9BE9C, F.Cu at (165.2, 88.5)
- moved R4 6.66 mm to (159.0, 88.5)
- moved R5 6.65 mm to (159.0, 86.5)
- moved R6 6.65 mm to (159.0, 84.5)
- moved R10 2.89 mm to (114.8, 68.2)
- moved R9 2.89 mm to (113.8, 68.2), turned to -90 degrees
- moved U2 2.75 mm to (111.8, 69.0)
- moved D4 2.68 mm to (161.0, 88.5)
- moved D5 2.68 mm to (161.0, 86.5)
- moved D6 2.68 mm to (161.0, 84.5)
- moved R11 2.50 mm to (109.2, 68.0), turned to 0 degrees
- moved R1 2.22 mm to (121.4, 77.0), turned to 0 degrees
- moved D2 1.53 mm to (116.2, 91.2), turned to 180 degrees
- moved D3 1.51 mm to (116.2, 92.7), turned to 180 degrees
- moved R3 1.10 mm to (115.6, 94.0), turned to 180 degrees
- moved R2 0.90 mm to (115.6, 90.0), turned to 180 degrees
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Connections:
- L1 pad 2: Net-(L1-Pad2) -> +3.3V
- R13 pad 1: Net-(L1-Pad2) -> +3.3V
- U4 pad 40: /SPI_CS_IMU_SEC1 -> /SPI_CS_MAG
- U4 pad 41: /SPI_CS_MAG -> /SPI_CS_IMU_SEC1
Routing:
- net GND: track 67.7 -> 132.9 mm, vias 47 -> 86
- net VBUS: track 0.00 -> 60.9 mm
- net /SPI_CS_IMU_PRI: track 0.00 -> 57.3 mm, vias 0 -> 2
- net /PIN_GPIO_BUZZER: track 0.00 -> 43.8 mm, vias 1 -> 2
- net /SPI_CS_MAG: track 0.00 -> 42.5 mm, vias 0 -> 2
- net /SPI_CS_IMU_SEC1: track 0.00 -> 39.2 mm, vias 0 -> 2
- net Net-(SW6-B): track 0.00 -> 36.1 mm, vias 0 -> 1
- net /SPI_CS_IMU_SEC0: track 0.00 -> 35.5 mm, vias 0 -> 2
- net /TRST: track 0.00 -> 33.6 mm, vias 0 -> 1
- net Net-(SW5-B): track 0.00 -> 33.6 mm, vias 0 -> 1
- net /SWD_TDO/SWO: track 0.00 -> 30.3 mm, vias 0 -> 2
- net /SWD_TDI: track 0.00 -> 26.7 mm, vias 0 -> 1
- net +3.3V: track 62.4 -> 89.0 mm, vias 29 -> 49
- net /USART2_RX: track 0.00 -> 24.1 mm
- net /I2C2_SDA: track 0.00 -> 22.5 mm, vias 0 -> 1
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- added copper zone on F.Cu, net +3.3V
- added copper zone on F.Cu, net +5V
- added copper zone on F.Cu, net /BUCKVIN
- added copper zone on F.Cu, net GND
- added copper zone on F.Cu, net Net-(U3-BST)
- added copper zone on F.Cu, net Net-(U3-FB)
- added copper zone on F.Cu, net Net-(U3-RT)
- added copper zone on F.Cu, net Net-(U3-SS)
- added copper zone on F.Cu, net Net-(U3-SW)

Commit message: Finish initial revision
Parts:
- added G***: LOGO, LOGO, B.Cu at (119.0, 62.5)
- added J2: Conn_ST_STDC14, Connector_PinHeader_2.54mm:PinHeader_2x07_P2.54mm_Vertical, F.Cu at (175.2, 56.9)
- added kibuzzard-69BF686D: G***, kibuzzard-69BF686D, F.Cu at (119.8, 92.6)
- added kibuzzard-69BF6875: G***, kibuzzard-69BF6875, F.Cu at (120.0, 91.2)
- added kibuzzard-69BF6ED0: G***, kibuzzard-69BF6ED0, F.Cu at (159.5, 76.0)
- added kibuzzard-69BF6ED7: G***, kibuzzard-69BF6ED7, F.Cu at (159.5, 81.0)
- added kibuzzard-69BF735A: G***, kibuzzard-69BF735A, B.Cu at (141.5, 59.3)
- added kibuzzard-69BF7398: G***, kibuzzard-69BF7398, B.Cu at (141.5, 62.2)
- added kibuzzard-69C071BD: G***, kibuzzard-69C071BD, B.Cu at (149.0, 66.5)
- added kibuzzard-69C071CC: G***, kibuzzard-69C071CC, B.Cu at (142.0, 70.0)
- added kibuzzard-69C071F5: G***, kibuzzard-69C071F5, B.Cu at (143.8, 73.5)
- TP14, TP15, TP16, TP17, TP18, TP19, TP20, TP21, TP22, TP23, TP24, TP6, TP7, TP8, TP9: moved to B.Cu
- U1: footprint Connector_PinSocket_2.54mm:PinSocket_2x10_P2.54mm_Vertical -> Connector_PinHeader_2.54mm:PinHeader_2x10_P2.54mm_Vertical
- moved TP10 111.9 mm to (171.9, 121.2)
- moved TP11 108.1 mm to (169.2, 121.2)
- moved TP4 103.0 mm to (163.2, 90.6)
- moved TP7 101.6 mm to (159.8, 118.1), turned to 180 degrees
- moved TP6 100.2 mm to (163.8, 86.0), turned to 180 degrees
- moved TP8 97.8 mm to (158.1, 114.4), turned to 180 degrees
- moved TP5 97.6 mm to (160.5, 90.6)
- moved TP13 96.8 mm to (160.5, 114.4)
- moved TP12 94.7 mm to (156.1, 121.3)
- moved TP9 94.0 mm to (156.7, 107.0), turned to 180 degrees
- moved TP16 77.2 mm to (147.5, 97.8), turned to 180 degrees
- moved TP19 73.8 mm to (147.5, 95.2), turned to 180 degrees
- moved TP18 73.5 mm to (147.4, 90.5), turned to 180 degrees
- moved TP17 73.3 mm to (147.4, 84.5), turned to 180 degrees
- moved TP20 71.7 mm to (145.2, 76.5), turned to 180 degrees
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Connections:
- C71 pad 1: +3V3 -> +3.3V
- C73 pad 1: +3V3 -> +3.3V
- U15 pad 5: +3V3 -> +3.3V
- U16 pad 5: +3V3 -> +3.3V
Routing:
- net /UART4_TX: track 0.00 -> 69.0 mm, vias 0 -> 3
- net /UART4_RX: track 0.00 -> 67.5 mm, vias 0 -> 3
- net /NRST: track 21.3 -> 85.0 mm, vias 2 -> 5
- net /Inertial Measurement System/INT_PRI_DRDY: track 0.00 -> 62.4 mm, vias 0 -> 2
- net /SWD_TMS/SWDIO: track 0.00 -> 53.1 mm, vias 0 -> 2
- net /STM32H747/FMCNBL1: track 0.00 -> 51.1 mm, vias 1 -> 4
- net /PIN_GPIO_CFG_0: track 2.26 -> 52.3 mm, vias 0 -> 2
- net /SWD_TRACE_D0: track 0.00 -> 45.0 mm, vias 0 -> 2
- net /I2C3_SCL: track 0.00 -> 44.5 mm, vias 0 -> 1
- net /SWD_TRACE_D1: track 0.00 -> 43.5 mm, vias 0 -> 2
- net /PIN_GPIO_CFG_2: track 1.98 -> 45.0 mm, vias 1 -> 2
- net /I2C3_SDA: track 0.00 -> 42.7 mm, vias 0 -> 1
- net /PIN_GPIO_CFG_1: track 0.00 -> 42.6 mm, vias 0 -> 3
- net /PIN_GPIO_CFG_3: track 1.78 -> 43.2 mm, vias 1 -> 2
- net /STM32H747/FMCNBL0: track 0.00 -> 40.1 mm, vias 0 -> 3
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- added copper zone on B.Cu, net GND
